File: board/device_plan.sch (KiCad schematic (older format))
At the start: 29 parts

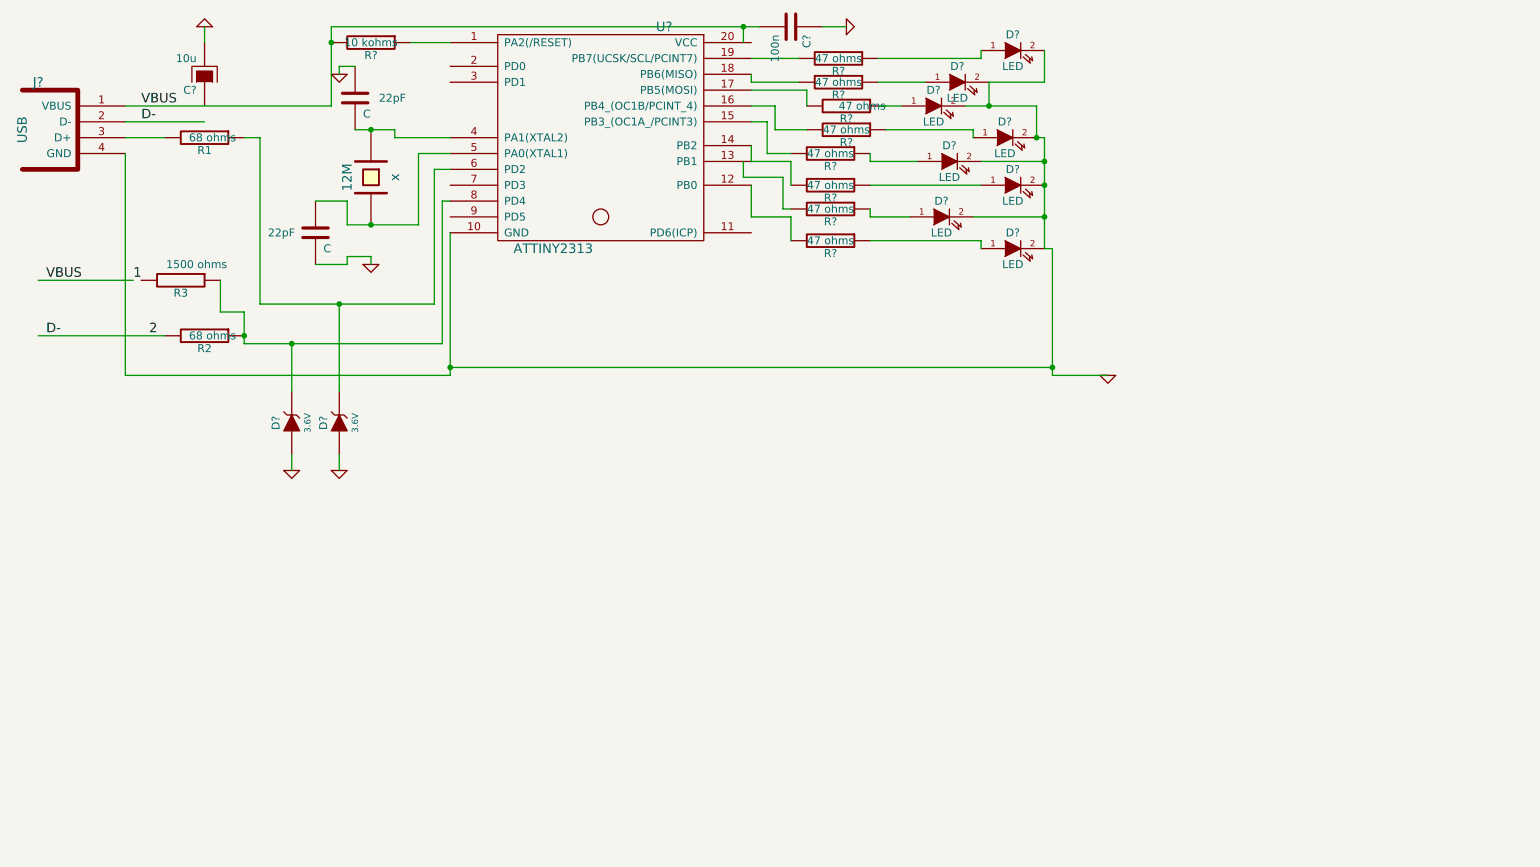
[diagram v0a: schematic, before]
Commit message: updated device_plan.sch  and usb_plug.lib ; added documents folder and images folder
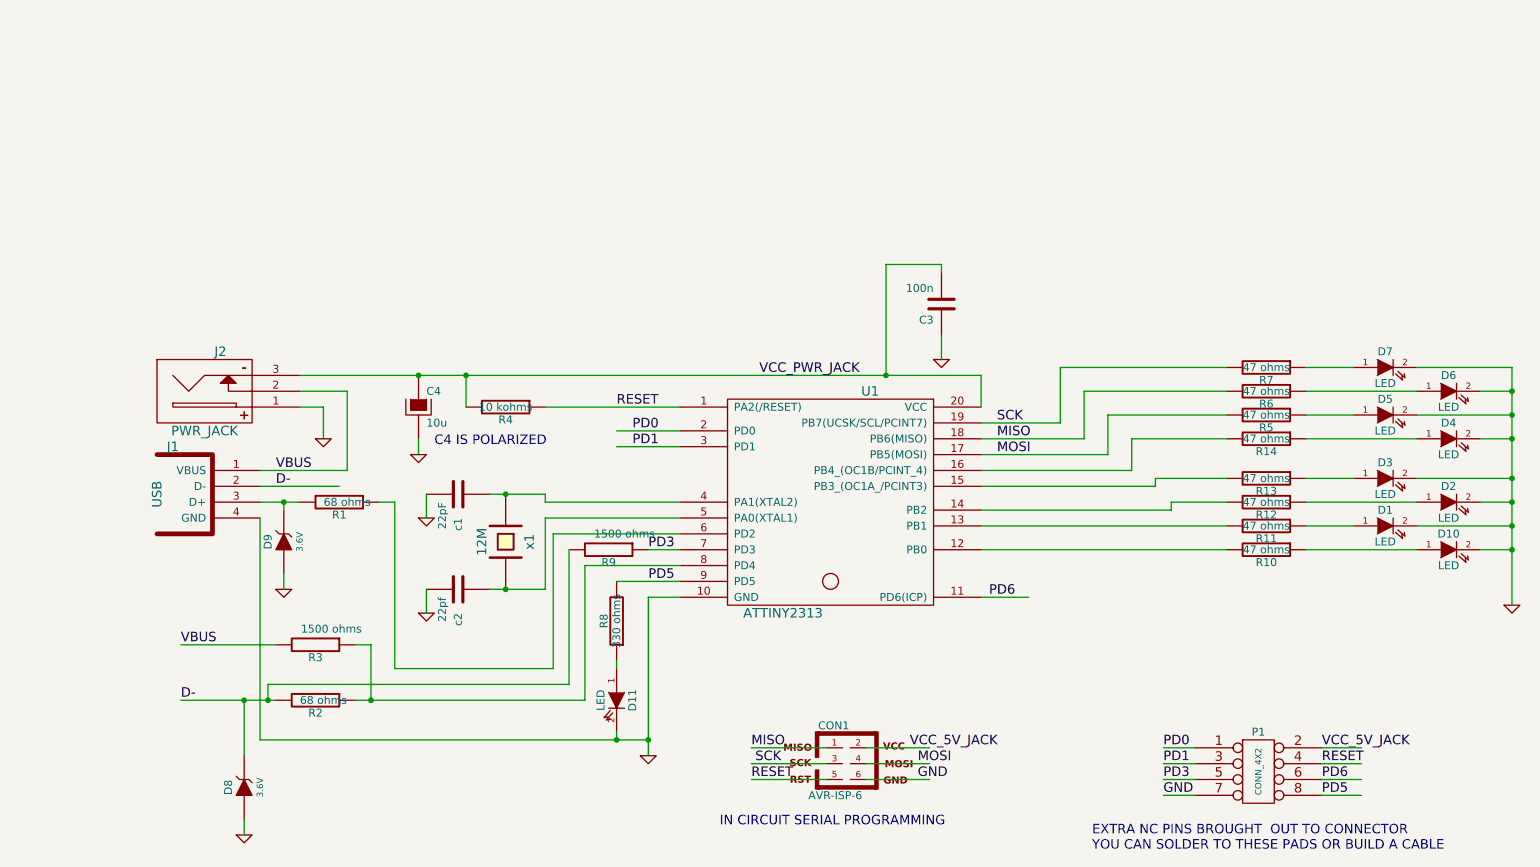
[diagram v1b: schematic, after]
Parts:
- removed U?: ATTINY2313, symbol ATTINY2313
- added CON1: AVR-ISP-6, AVR-ISP-6, symbol AVR-ISP-6
- added D11: LED, symbol LED
- added J2: PWR_JACK, symbol PWR_JACK
- added P1: CONN_4X2, symbol CONN_4X2
- added R8: 330 ohms, symbol R
- added R9: 1500 ohms, symbol R
- added U1: ATTINY2313, symbol ATTINY2313
- c1: renamed from 22pF; value C -> 22pF
- c2: renamed from 22pF; value C -> 22pf
- gave numbers to parts that had none: 22
- renumbered x to x1
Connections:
- net labels added: MISO, MOSI, PD0, PD1, PD3, PD5, PD6, RESET, SCK, VCC_5V_JACK, VCC_PWR_JACK
- net labels removed: 1, 2
- wire segments 90 -> 105
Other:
- note added: "C4 IS POLARIZED\n"
- note added: "EXTRA NC PINS BROUGHT OUT TO CONNECTOR\nYOU CAN SOLDER TO THESE PADS OR BUILD A CABLE\n\n"
- note added: "IN CIRCUIT SERIAL PROGRAMMING\n"
- moved on the sheet: C3, C4, D1, D10, D2, D3, D4, D5, D6, D7, D8, D9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
